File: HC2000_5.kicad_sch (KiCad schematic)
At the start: 12 parts

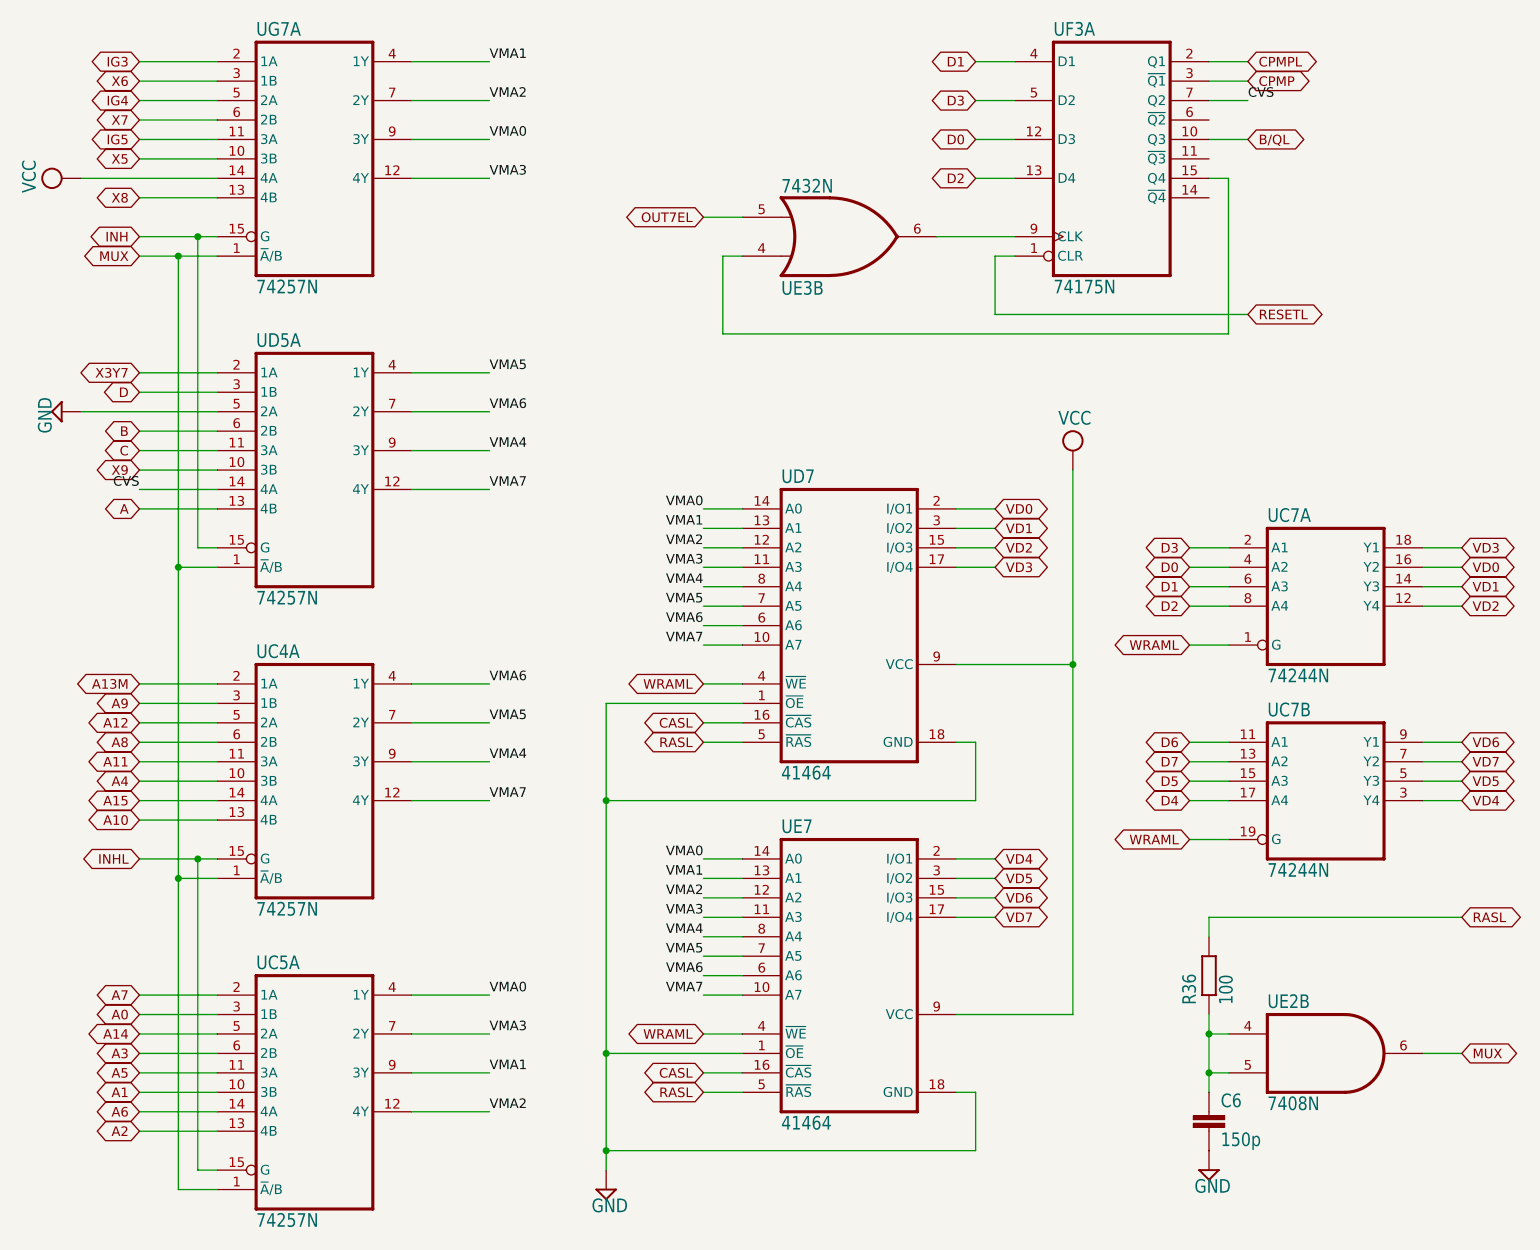
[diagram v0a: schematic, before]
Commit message: Fix errors (IC & unnoticed cut for 1 EPROM)
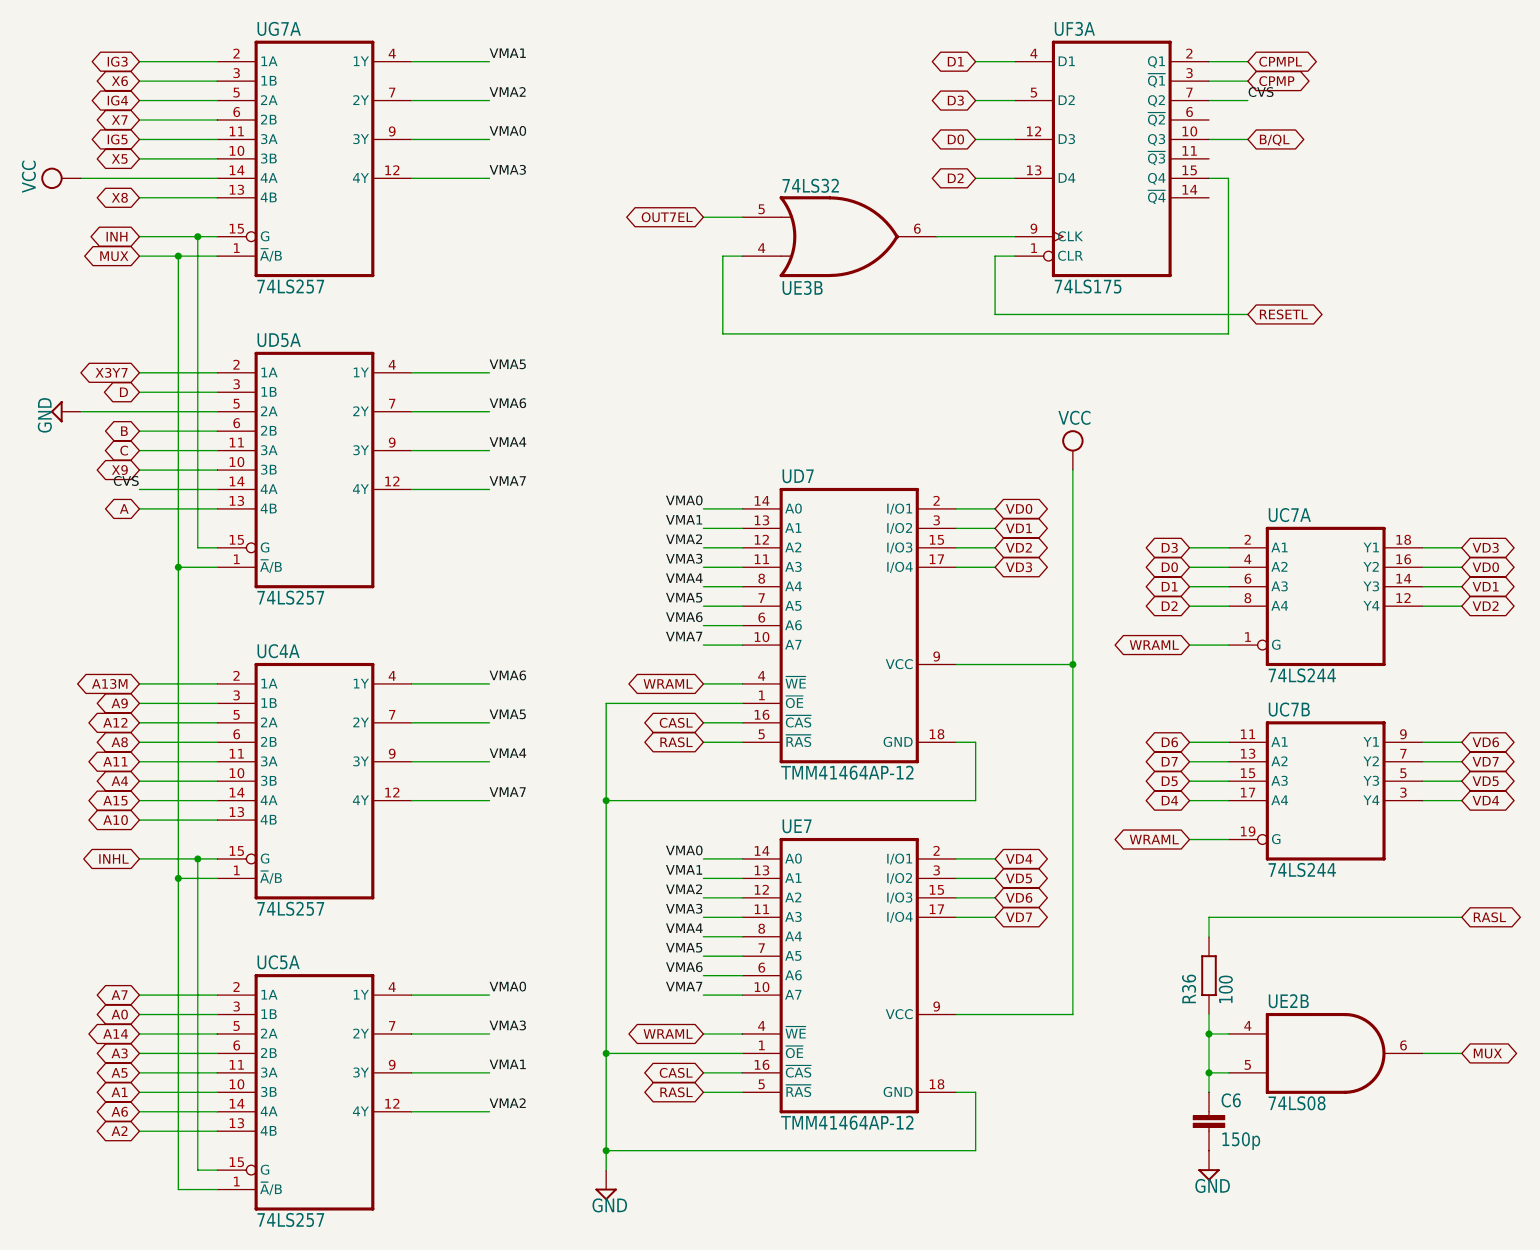
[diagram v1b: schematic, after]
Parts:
- UC4, UC5, UD5, UG7: value 74257N -> 74LS257
- UC7: value 74244N -> 74LS244
- UD7, UE7: value 41464 -> TMM41464AP-12
- UE2: value 7408N -> 74LS08
- UE3: value 7432N -> 74LS32
- UF3: value 74175N -> 74LS175
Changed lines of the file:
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@@
       (effects (font (size 1.778 1.5113)) (justify left bottom))
     )
-    (property "Value" "74257N" (at 81.28 101.6 0)
+    (property "Value" "74LS257" (at 81.28 101.6 0)
       (effects (font (size 1.778 1.5113)) (justify left bottom))
     )
@@
       (effects (font (size 1.778 1.5113)) (justify left bottom))
     )
-    (property "Value" "41464" (at 149.86 170.18 0)
+    (property "Value" "TMM41464AP-12" (at 149.86 170.18 0)
       (effects (font (size 1.778 1.5113)) (justify left bottom))
     )
@@
       (effects (font (size 1.778 1.5113)) (justify left bottom))
     )
-    (property "Value" "7408N" (at 213.36 167.64 0)
+    (property "Value" "74LS08" (at 213.36 167.64 0)
       (effects (font (size 1.778 1.5113)) (justify left bottom))
     )
@@
       (effects (font (size 1.778 1.5113)) (justify left bottom))
     )
-    (property "Value" "74257N" (at 81.28 60.96 0)
+    (property "Value" "74LS257" (at 81.28 60.96 0)
       (effects (font (size 1.778 1.5113)) (justify left bottom))
     )
@@
       (effects (font (size 1.778 1.5113)) (justify left bottom))
     )
-    (property "Value" "74244N" (at 213.36 111.76 0)
+    (property "Value" "74LS244" (at 213.36 111.76 0)
       (effects (font (size 1.778 1.5113)) (justify left bottom))
     )
@@
       (effects (font (size 1.778 1.5113)) (justify left bottom))
     )
-    (property "Value" "74257N" (at 81.28 182.88 0)
+    (property "Value" "74LS257" (at 81.28 182.88 0)
       (effects (font (size 1.778 1.5113)) (justify left bottom))
     )
@@
       (effects (font (size 1.778 1.5113)) (justify left bottom))
     )
-    (property "Value" "74175N" (at 185.42 60.96 0)
+    (property "Value" "74LS175" (at 185.42 60.96 0)
       (effects (font (size 1.778 1.5113)) (justify left bottom))
     )
@@
       (effects (font (size 1.778 1.5113)) (justify left bottom))
     )
-    (property "Value" "74244N" (at 213.36 137.16 0)
+    (property "Value" "74LS244" (at 213.36 137.16 0)
       (effects (font (size 1.778 1.5113)) (justify left bottom))
     )
@@
       (effects (font (size 1.778 1.5113)) (justify left bottom))
     )
-    (property "Value" "41464" (at 149.86 124.46 0)
+    (property "Value" "TMM41464AP-12" (at 149.86 124.46 0)
       (effects (font (size 1.778 1.5113)) (justify left bottom))
     )
@@
       (effects (font (size 1.778 1.5113)) (justify left bottom))
     )
-    (property "Value" "74257N" (at 81.28 142.24 0)
+    (property "Value" "74LS257" (at 81.28 142.24 0)
       (effects (font (size 1.778 1.5113)) (justify left bottom))
     )
@@
       (effects (font (size 1.778 1.5113)) (justify left bottom))
     )
-    (property "Value" "7432N" (at 149.86 45.72 0)
-      (effects (font (size 1.778 1.5113)) (justify left bottom))
-    )
+    (property "Value" "74LS32" (at 149.86 45.72 0)
+      (effects (font (size 1.778 1.5113)) (justify left bottom))
+    )

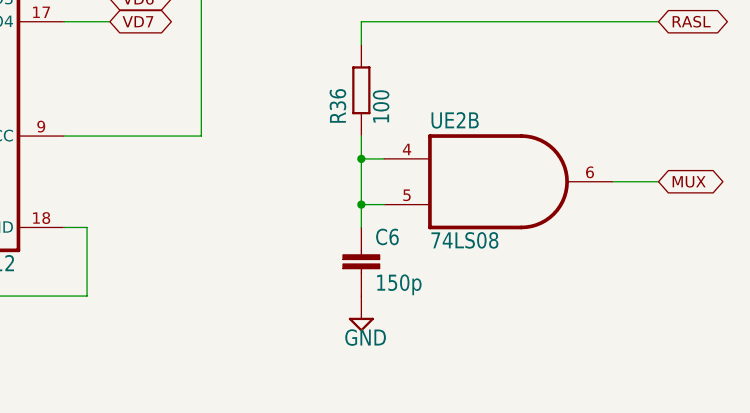
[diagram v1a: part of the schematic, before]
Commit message: A few minor changes
R62 has value 470 instead of 910 and C6 is missing.
Connected a few conector's shield pins to GND.
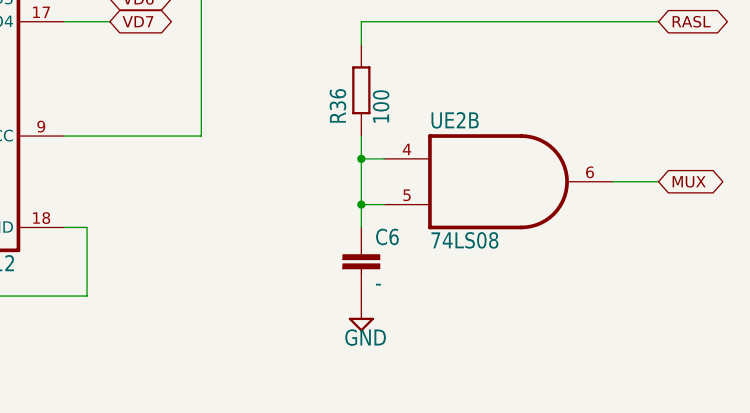
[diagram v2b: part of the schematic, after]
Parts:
- C6: value 150p -> -
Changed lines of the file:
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@@
       (effects (font (size 1.778 1.5113)) (justify left bottom))
     )
-    (property "Value" "150p" (at 207.264 172.339 0)
+    (property "Value" "-" (at 207.264 172.339 0)
       (effects (font (size 1.778 1.5113)) (justify left bottom))
     )
